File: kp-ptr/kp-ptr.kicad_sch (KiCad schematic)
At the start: 36 parts, among them J1 ESP32_PROG_CON, U1 ESP32-S3, Y1 7M40000005-40MHz

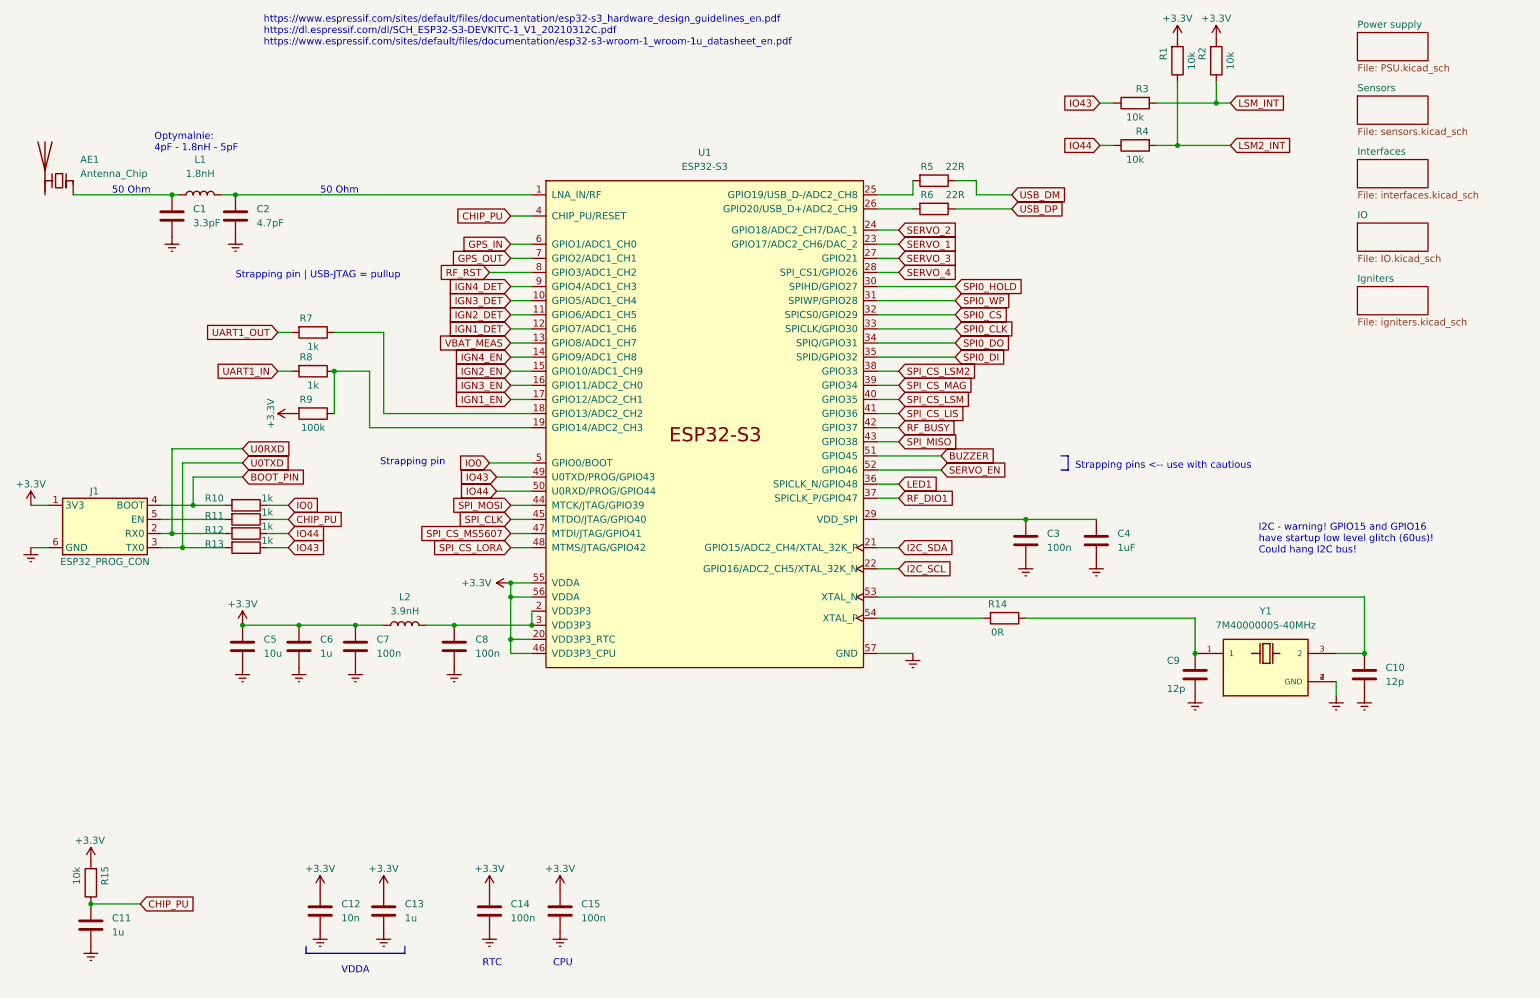
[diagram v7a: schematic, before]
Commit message: + Kicad update to 9.0
+ CC resistors added
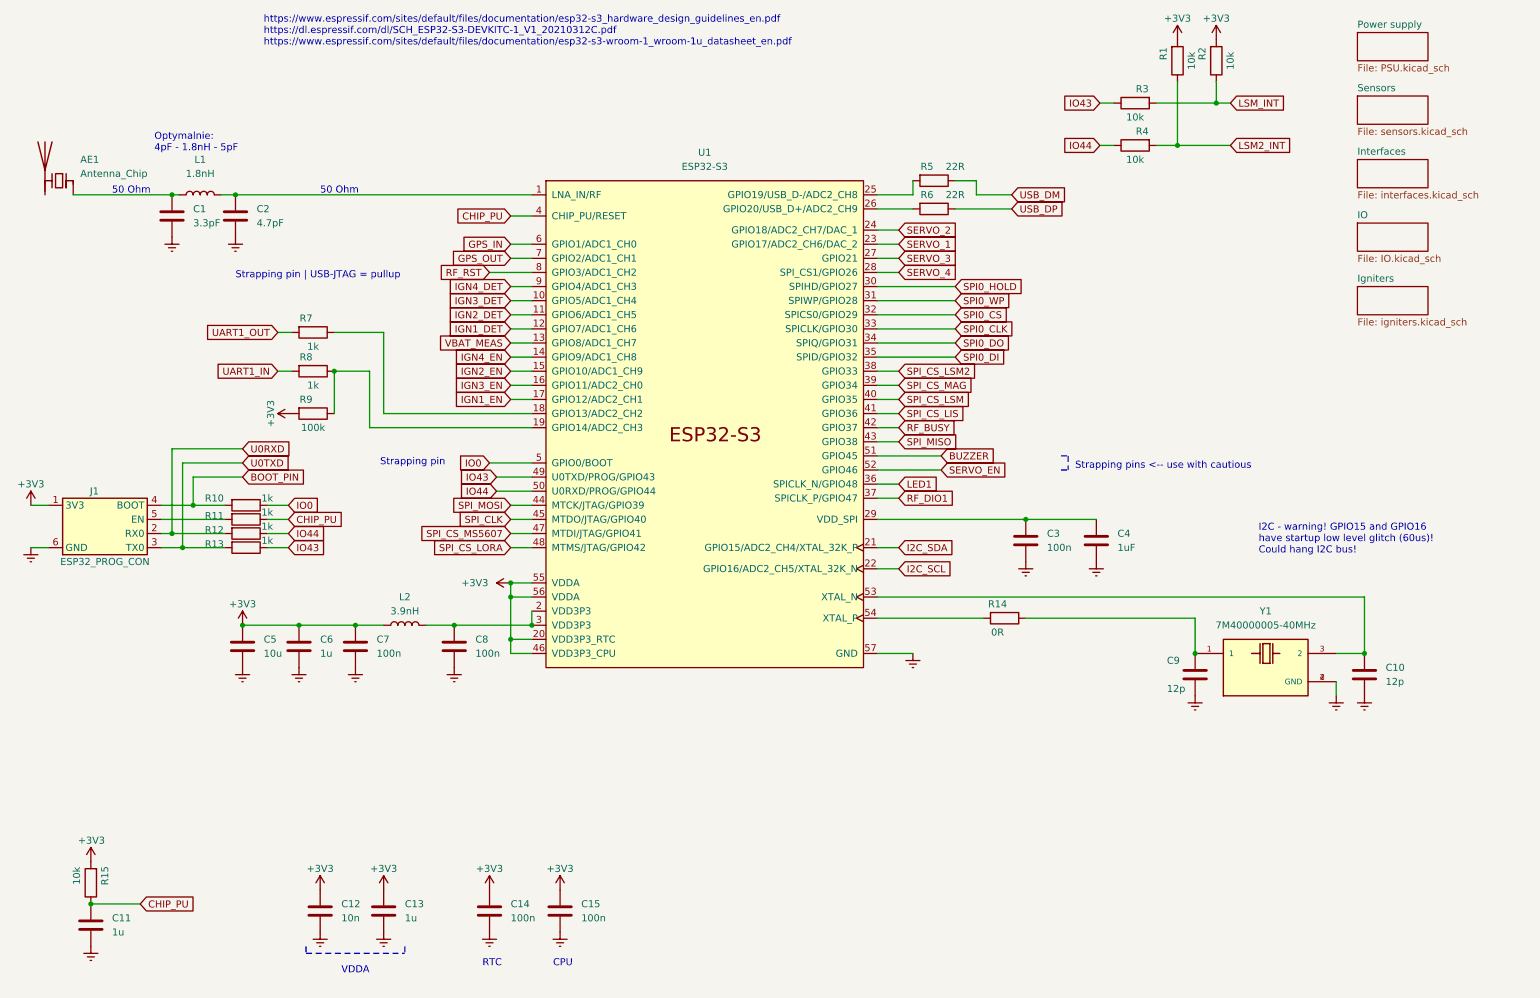
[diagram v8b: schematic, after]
